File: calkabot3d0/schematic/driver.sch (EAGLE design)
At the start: 48 parts

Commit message: teraz schemat wygląda ładnie
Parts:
- removed SDA: (no value), pinhead:PINHD-1X2
- added C15: (no value), rcl:C-EUC0603
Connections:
- new net N$13: C15.1, STM32AN_POWER.VBAT
- net GND: now also C15.2
- net SCL: no longer SDA.1
- net SDA: no longer SDA.2
- net VCC: no longer R14.2
- net VDD: now also R14.2; no longer STM32AN_POWER.VBAT
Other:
- moved on the sheet: 12V, 3.3V, C1, C10, C11, C12, C13, C14, C2, C3, C4, C5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

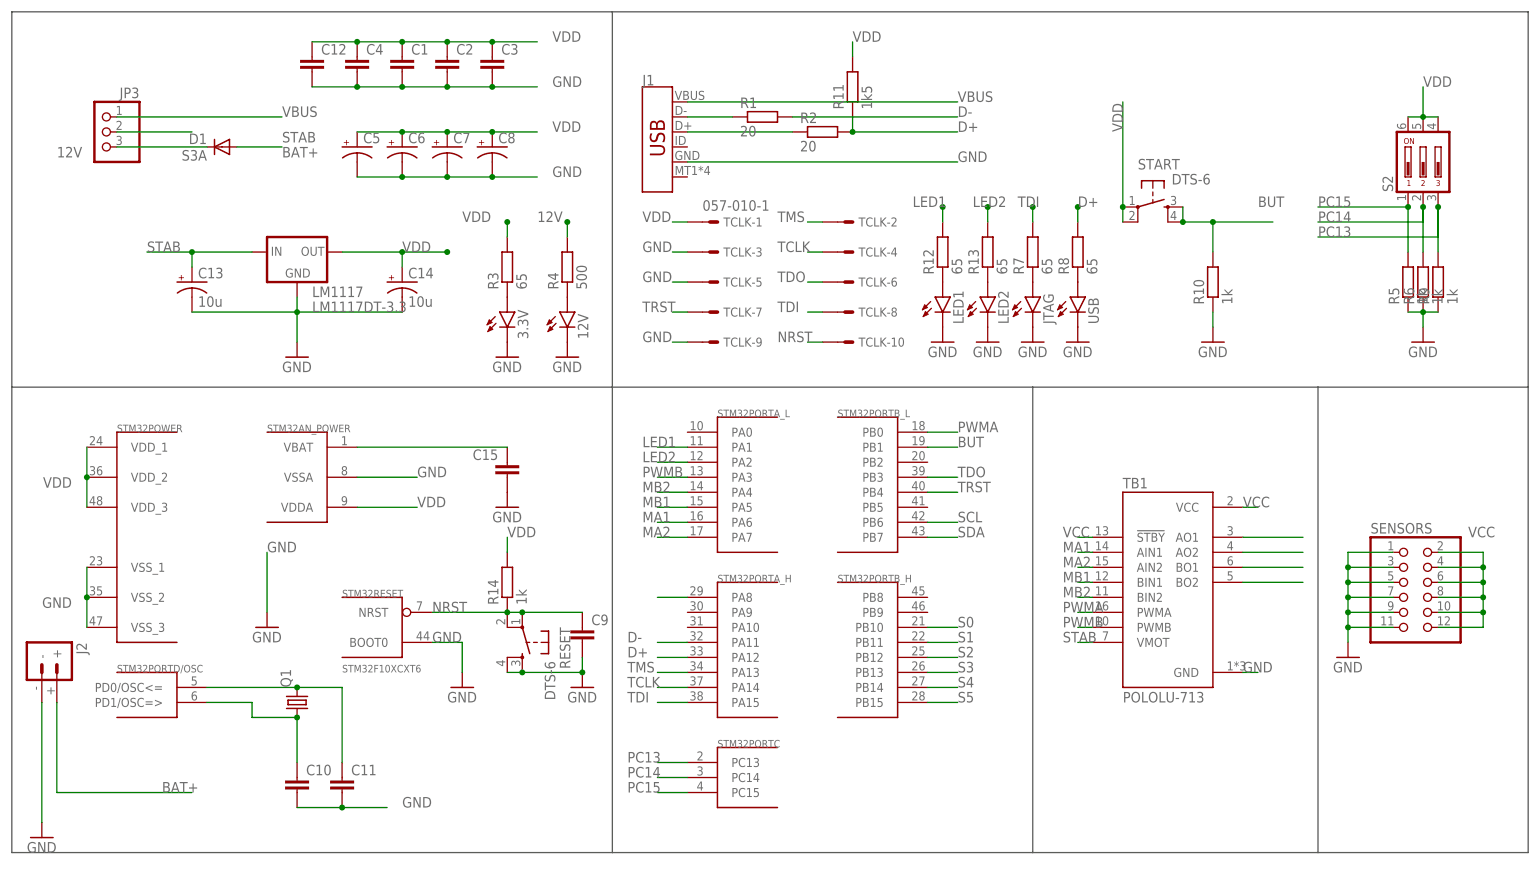
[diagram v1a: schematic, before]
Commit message: Jtag ssie, zrobiłem SWD. Zmiana płyki. pomniejszenie dodanie resetu itd.
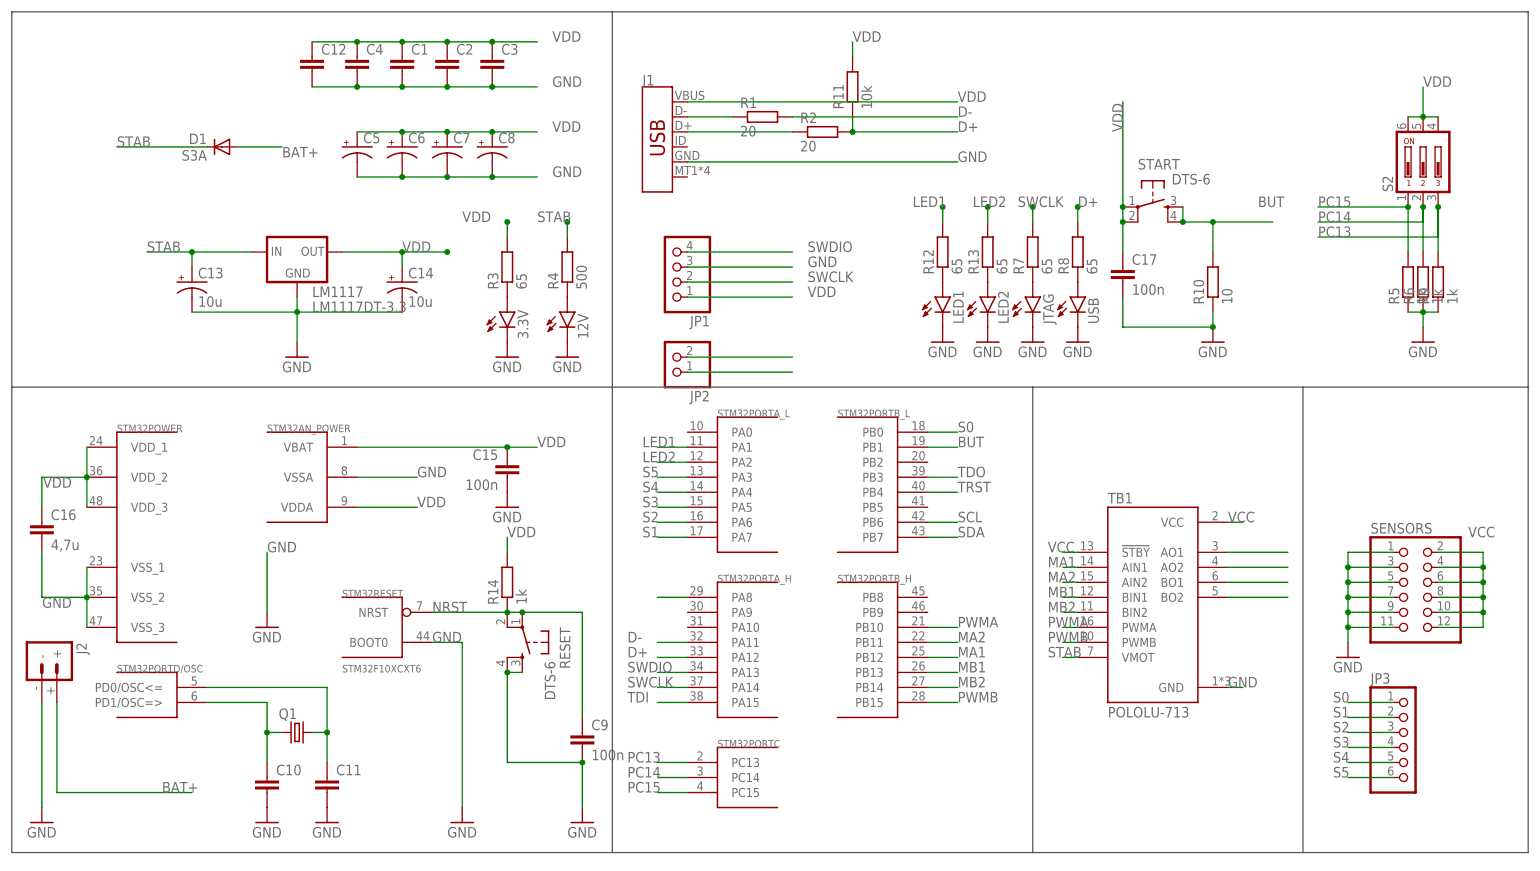
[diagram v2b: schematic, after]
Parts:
- removed TCLK: 057-010-1, con-panduit:057-010-1
- added C16: 4,7u, rcl:C-EUC0603
- added C17: 100n, rcl:C-EUC0603
- added JP1: (no value), pinhead:PINHD-1X4
- added JP2: (no value), pinhead:PINHD-1X2
- 12V, 3.3V, JTAG, LED1, LED2, USB: device led:LEDSML0603 -> led:LEDCHIPLED_0805
- C15, C9: value (none) -> 100n
- JP3: device pinhead:PINHD-1X3 -> pinhead:PINHD-1X6
- R1, R12, R13, R14, R2, R3, R4, R5, R6, R7, R8, R9: device rcl:R-EU_R0603 -> rcl:R-EU_R0805
- R10: value 1k -> 10; device rcl:R-EU_R0603 -> rcl:R-EU_R0805
- R11: value 1k5 -> 10k; device rcl:R-EU_R0603 -> rcl:R-EU_R0805
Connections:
- removed net 12V: D1.C, JP3.3, R4.2
- removed net TCLK: STM32PORTA_H.PA14, TCLK-4.S
- removed net TMS: STM32PORTA_H.PA13, TCLK-2.S
- removed net VBUS: J1.VBUS, JP3.1
- new net N$14: JP2.1
- new net SWCLK: JP1.2, R7.2, STM32PORTA_H.PA14
- new net SWDIO: JP1.4, STM32PORTA_H.PA13
- net GND: now also C16.2, C17.2, JP1.3; no longer TCLK-3.S, TCLK-5.S, TCLK-9.S
- net MA1: now also STM32PORTB_H.PB12; no longer STM32PORTA_L.PA6
- net MA2: now also STM32PORTB_H.PB11; no longer STM32PORTA_L.PA7
- net MB1: now also STM32PORTB_H.PB13; no longer STM32PORTA_L.PA5
- net MB2: now also STM32PORTB_H.PB14; no longer STM32PORTA_L.PA4
- net N$13: now also JP2.2; no longer C15.1, STM32AN_POWER.VBAT
- net N$3: now also Q1.1; no longer Q1.2
- net N$4: now also Q1.2; no longer Q1.1
- net NRST: no longer TCLK-10.S
- net PWMA: now also STM32PORTB_H.PB10; no longer STM32PORTB_L.PB0
- net PWMB: now also STM32PORTB_H.PB15; no longer STM32PORTA_L.PA3
- net S0: now also JP3.1, STM32PORTB_L.PB0; no longer STM32PORTB_H.PB10
- net S1: now also JP3.2, STM32PORTA_L.PA7; no longer STM32PORTB_H.PB11
- net S2: now also JP3.3, STM32PORTA_L.PA6; no longer STM32PORTB_H.PB12
- net S3: now also JP3.4, STM32PORTA_L.PA5; no longer STM32PORTB_H.PB13
- net S4: now also JP3.5, STM32PORTA_L.PA4; no longer STM32PORTB_H.PB14
- net S5: now also JP3.6, STM32PORTA_L.PA3; no longer STM32PORTB_H.PB15
- net STAB: now also D1.C, R4.2; no longer JP3.2
- net TDI: no longer R7.2, TCLK-8.S
- net TDO: no longer TCLK-6.S
- net TRST: no longer TCLK-7.S
- net VDD: now also C15.1, C16.1, C17.1, J1.VBUS, JP1.1, STM32AN_POWER.VBAT; no longer TCLK-1.S
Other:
- moved on the sheet: C10, C11, C9, Q1, TB1

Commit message: Adding I2C pull-up resistors, 5V on board, change package for LM1117, PB2 (BOOT1) short to GND
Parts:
- added C18, C19: 10u, rcl:CPOL-USCT3528
- added LM1: LM1117MP-3.3, lm1117_11:LM1117MP-3.3
- added R15, R16: 4k7, rcl:R-EU_R0805
- JP2: device pinhead:PINHD-1X2 -> pinhead:PINHD-1X4
- LM1117: value LM1117DT-3.3 -> LM1117MP-3.3; device lm1117_10:LM1117DT-3.3 -> lm1117_11:LM1117MP-3.3
- R10: value 10 -> 10k
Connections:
- removed net N$13: JP2.2
- removed net N$14: JP2.1
- new net SWDA: JP1.2
- net GND: now also C18.-, C19.-, JP1.4, JP2.3, LM1.GND, STM32PORTB_L.PB2; no longer JP1.3
- net SCL: now also JP2.2, R16.1
- net SDA: now also JP2.1, R15.1
- net STAB: now also C18.+, LM1.IN
- net SWCLK: now also JP1.3; no longer JP1.2
- net SWDIO: no longer JP1.4
- net VCC: now also C19.+, JP2.4, LM1.OUT, R15.2, R16.2
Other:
- moved on the sheet: C13, C14, LM1117

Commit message: Adding motor outputs
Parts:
- removed JP3: (no value), pinhead:PINHD-1X6
- removed SENSORS: (no value), pinhead:PINHD-2X6
- added JP4, JP5: (no value), pinhead:PINHD-1X2/90
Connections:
- net GND: no longer SENSORS.1, SENSORS.11, SENSORS.3, SENSORS.5, SENSORS.7, SENSORS.9
- net N$42: now also JP4.2
- net N$43: now also JP4.1
- net N$44: now also JP5.2
- net N$45: now also JP5.1
- net S0: no longer JP3.1
- net S1: no longer JP3.2
- net S2: no longer JP3.3
- net S3: no longer JP3.4
- net S4: no longer JP3.5
- net S5: no longer JP3.6
- net VCC: no longer SENSORS.10, SENSORS.12, SENSORS.2, SENSORS.4, SENSORS.6, SENSORS.8
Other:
- moved on the sheet: 12V, 3.3V, C1, C10, C11, C12, C13, C14, C15, C16, C17, C18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

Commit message: Change board
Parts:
- renumbered JP1 to SWD, JP2 to I2C
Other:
- moved on the sheet: R11
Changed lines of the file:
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@@
 <part name="GND17" library="supply1" library_urn="urn:adsk.eagle:library:371" deviceset="GND" device=""/>
 <part name="C16" library="rcl" library_urn="urn:adsk.eagle:library:334" deviceset="C-EU" device="C0603" package3d_urn="urn:adsk.eagle:package:23616/2" value="4,7u"/>
-<part name="JP1" library="pinhead" library_urn="urn:adsk.eagle:library:325" deviceset="PINHD-1X4" device="" package3d_urn="urn:adsk.eagle:package:22407/2"/>
+<part name="SWD" library="pinhead" library_urn="urn:adsk.eagle:library:325" deviceset="PINHD-1X4" device="" package3d_urn="urn:adsk.eagle:package:22407/2"/>
 <part name="C17" library="rcl" library_urn="urn:adsk.eagle:library:334" deviceset="C-EU" device="C0603" package3d_urn="urn:adsk.eagle:package:23616/2" value="100n"/>
 <part name="LM1" library="lm1117_11" deviceset="LM1117?-*" device="MP" override_package3d_urn="urn:adsk.eagle:package:17629158/3" override_package_urn="urn:adsk.eagle:footprint:17629160/1" override_locally_modified="yes" technology="3.3"/>
@@
 <part name="C18" library="rcl" library_urn="urn:adsk.eagle:library:334" deviceset="CPOL-US" device="CT3528" package3d_urn="urn:adsk.eagle:package:23325/2" value="10u"/>
 <part name="C19" library="rcl" library_urn="urn:adsk.eagle:library:334" deviceset="CPOL-US" device="CT3528" package3d_urn="urn:adsk.eagle:package:23325/2" value="10u"/>
-<part name="JP2" library="pinhead" library_urn="urn:adsk.eagle:library:325" deviceset="PINHD-1X4" device="" package3d_urn="urn:adsk.eagle:package:22407/2"/>
+<part name="I2C" library="pinhead" library_urn="urn:adsk.eagle:library:325" deviceset="PINHD-1X4" device="" package3d_urn="urn:adsk.eagle:package:22407/2"/>
 <part name="GND19" library="supply1" library_urn="urn:adsk.eagle:library:371" deviceset="GND" device=""/>
 <part name="R16" library="rcl" library_urn="urn:adsk.eagle:library:334" deviceset="R-EU_" device="R0805" package3d_urn="urn:adsk.eagle:package:23553/2" value="4k7"/>
@@
 <attribute name="VALUE" x="-80.01" y="110.998" size="1.778" layer="96"/>
 </instance>
-<instance part="R11" gate="G$1" x="-71.12" y="121.92" smashed="yes" rot="R90">
-<attribute name="NAME" x="-72.6186" y="118.11" size="1.778" layer="95" rot="R90"/>
-<attribute name="VALUE" x="-67.818" y="118.11" size="1.778" layer="96" rot="R90"/>
+<instance part="R11" gate="G$1" x="-71.12" y="127" smashed="yes" rot="R90">
+<attribute name="NAME" x="-72.6186" y="123.19" size="1.778" layer="95" rot="R90"/>
+<attribute name="VALUE" x="-67.818" y="123.19" size="1.778" layer="96" rot="R90"/>
 </instance>
 <instance part="J1" gate="J1" x="-104.14" y="111.76" smashed="yes">
@@
 <attribute name="VALUE" x="-282.956" y="43.561" size="1.778" layer="96"/>
 </instance>
-<instance part="JP1" gate="A" x="-106.68" y="96.52" smashed="yes" rot="R180">
+<instance part="SWD" gate="A" x="-106.68" y="96.52" smashed="yes" rot="R180">
 <attribute name="NAME" x="-100.33" y="88.265" size="1.778" layer="95" rot="R180"/>
 <attribute name="VALUE" x="-100.33" y="104.14" size="1.778" layer="96" rot="R180"/>
@@
 <attribute name="VALUE" x="-230.124" y="89.789" size="1.778" layer="96"/>
 </instance>
-<instance part="JP2" gate="A" x="-40.64" y="116.84" smashed="yes" rot="R180">
+<instance part="I2C" gate="A" x="-40.64" y="116.84" smashed="yes" rot="R180">
 <attribute name="NAME" x="-34.29" y="108.585" size="1.778" layer="95" rot="R180"/>
 <attribute name="VALUE" x="-34.29" y="124.46" size="1.778" layer="96" rot="R180"/>
@@
 <segment>
 <pinref part="R11" gate="G$1" pin="2"/>
-<wire x1="-71.12" y1="127" x2="-71.12" y2="129.54" width="0.1524" layer="91"/>
-<label x="-71.12" y="129.54" size="1.778" layer="95"/>
+<wire x1="-71.12" y1="132.08" x2="-71.12" y2="129.54" width="0.1524" layer="91"/>
+<label x="-71.12" y="134.62" size="1.778" layer="95"/>
 </segment>
 <segment>
@@
 </segment>
 <segment>
-<pinref part="JP1" gate="A" pin="1"/>
+<pinref part="SWD" gate="A" pin="1"/>
 <wire x1="-104.14" y1="91.44" x2="-86.36" y2="91.44" width="0.1524" layer="91"/>
 <label x="-83.82" y="91.44" size="1.778" layer="95"/>
@@
 <label x="-53.34" y="114.3" size="1.778" layer="95"/>
 <wire x1="-71.12" y1="114.3" x2="-53.34" y2="114.3" width="0.1524" layer="91"/>
-<wire x1="-71.12" y1="114.3" x2="-71.12" y2="116.84" width="0.1524" layer="91"/>
+<wire x1="-71.12" y1="114.3" x2="-71.12" y2="121.92" width="0.1524" layer="91"/>
 <junction x="-71.12" y="114.3"/>
 <pinref part="R11" gate="G$1" pin="1"/>
@@
 </segment>
 <segment>
-<pinref part="JP1" gate="A" pin="4"/>
+<pinref part="SWD" gate="A" pin="4"/>
 <wire x1="-104.14" y1="99.06" x2="-86.36" y2="99.06" width="0.1524" layer="91"/>
 <label x="-83.82" y="99.06" size="1.778" layer="95"/>
 </segment>
 <segment>
-<pinref part="JP2" gate="A" pin="3"/>
+<pinref part="I2C" gate="A" pin="3"/>
 <wire x1="-38.1" y1="116.84" x2="-22.86" y2="116.84" width="0.1524" layer="91"/>
 <label x="-22.86" y="116.84" size="1.778" layer="95"/>
@@
 </segment>
 <segment>
-<pinref part="JP2" gate="A" pin="2"/>
+<pinref part="I2C" gate="A" pin="2"/>
 <wire x1="-38.1" y1="114.3" x2="-22.86" y2="114.3" width="0.1524" layer="91"/>
 <label x="-22.86" y="114.3" size="1.778" layer="95"/>
@@
 </segment>
 <segment>
-<pinref part="JP2" gate="A" pin="1"/>
+<pinref part="I2C" gate="A" pin="1"/>
 <wire x1="-38.1" y1="111.76" x2="-22.86" y2="111.76" width="0.1524" layer="91"/>
 <label x="-22.86" y="111.76" size="1.778" layer="95"/>
@@
 </segment>
 <segment>
-<pinref part="JP2" gate="A" pin="4"/>
+<pinref part="I2C" gate="A" pin="4"/>
 <wire x1="-38.1" y1="119.38" x2="-22.86" y2="119.38" width="0.1524" layer="91"/>
 <label x="-22.86" y="119.38" size="1.778" layer="95"/>
@@
 </segment>
 <segment>
-<pinref part="JP1" gate="A" pin="3"/>
+<pinref part="SWD" gate="A" pin="3"/>
 <wire x1="-104.14" y1="96.52" x2="-86.36" y2="96.52" width="0.1524" layer="91"/>
 <label x="-83.82" y="96.52" size="1.778" layer="95"/>
@@
 <net name="SWDA" class="0">
 <segment>
-<pinref part="JP1" gate="A" pin="2"/>
+<pinref part="SWD" gate="A" pin="2"/>
 <wire x1="-104.14" y1="93.98" x2="-86.36" y2="93.98" width="0.1524" layer="91"/>
 <label x="-83.82" y="93.98" size="1.778" layer="95"/>
